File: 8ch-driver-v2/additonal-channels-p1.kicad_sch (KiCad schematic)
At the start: 42 parts, among them Q3 2N7002E, Q4 2N7002E, Q5 2N7002E, U3 DRV104PWP, U4 DRV104PWP, U5 DRV104PWP

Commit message: progress
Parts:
- renumbered Q5 to Q3, Q3 to Q5
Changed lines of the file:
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@@
 		(dnp no)
 		(fields_autoplaced yes)
-		(property "Reference" "Q5"
+		(property "Reference" "Q3"
 			(at 34.29 181.61 0)
 			(effects
@@
 			(project "8ch-driver-v2"
 				(path "/a0da8170-9d86-479a-b2aa-1f6179555439/fa1b9fcd-d6e8-44ab-a3c7-d4c590cf5d5a"
-					(reference "Q5")
+					(reference "Q3")
 					(unit 1)
 				)
@@
 		(dnp no)
 		(fields_autoplaced yes)
-		(property "Reference" "Q3"
+		(property "Reference" "Q5"
 			(at 33.02 73.66 0)
 			(effects
@@
 			(project "8ch-driver-v2"
 				(path "/a0da8170-9d86-479a-b2aa-1f6179555439/fa1b9fcd-d6e8-44ab-a3c7-d4c590cf5d5a"
-					(reference "Q3")
+					(reference "Q5")
 					(unit 1)
 				)

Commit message: mucho mas progresso
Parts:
- removed C10, C13, C16: 10uF, Capacitor_SMD:C_1210_3225Metric, symbol Device:C
- removed C11, C14, C8: 0.18uF, Capacitor_SMD:C_1206_3216Metric, symbol Device:C_Small
- removed C12, C15, C9: 470pF, Capacitor_SMD:C_1206_3216Metric, symbol Device:C_Small
- removed D10, D6, D8: PMEG10010ELRX, Diode_SMD:Nexperia_CFP3_SOD-123W, symbol Device:D
- removed D19, D20, D21: LED Green, LED_SMD:LED_0805_2012Metric, symbol Device:LED
- removed D7, D9: LED, LED_SMD:LED_0805_2012Metric, symbol Device:LED
- removed Q3, Q4, Q5: 2N7002E, Package_TO_SOT_SMD:SOT-23, symbol Transistor_FET:2N7002E
- removed R13, R17, R18, R22, R23: 4k7, Resistor_SMD:R_1206_3216Metric, symbol Device:R_US
- removed R14, R19, R24: 162k, Resistor_SMD:R_1206_3216Metric, symbol Device:R_US
- removed R15, R20, R25: 191k, Resistor_SMD:R_1206_3216Metric, symbol Device:R_US
- removed R16, R21: 49R9, Resistor_SMD:R_1206_3216Metric, symbol Device:R_US
- removed R43, R44, R45: 10K, Resistor_SMD:R_1206_3216Metric, symbol Device:R_US
- removed U3, U4, U5: DRV104PWP, Solenoid_Driver:IC_TPS27S100BPWPR, symbol DRV104PWP:DRV104PWP
- added C5: 10uF, Capacitor_SMD:C_1210_3225Metric, symbol Device:C
- added C6: 0.18uF, Capacitor_SMD:C_1206_3216Metric, symbol Device:C_Small
- added C7: 470pF, Capacitor_SMD:C_1206_3216Metric, symbol Device:C_Small
- added D4: PMEG10010ELRX, Diode_SMD:Nexperia_CFP3_SOD-123W, symbol Device:D
- added D6: LED, LED_SMD:LED_0805_2012Metric, symbol Device:LED
- added Q2: 2N7002E, Package_TO_SOT_SMD:SOT-23, symbol Transistor_FET:2N7002E
- added R10: 4k7, Resistor_SMD:R_1206_3216Metric, symbol Device:R_US
- added R7: 10K, Resistor_SMD:R_1206_3216Metric, symbol Device:R_US
- added R8: 162k, Resistor_SMD:R_1206_3216Metric, symbol Device:R_US
- added R9: 49R9, Resistor_SMD:R_1206_3216Metric, symbol Device:R_US
- added U2: DRV104PWP, Solenoid_Driver:IC_TPS27S100BPWPR, symbol DRV104PWP:DRV104PWP
- D5: value LED -> LED Green
- R11: value 49R9 -> 191k; PartNum RC0805FR-0749R9L -> RC0805FR-07191KL
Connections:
- net Relay03 is gone; now on net GND: R11.1
- net +12V: now also C5.1, R7.1, U2.10 (+VS), U2.8 (VPS2), U2.9 (VPS1)
- net GND: now also C5.2, C6.1, C7.1, D4.2 (A), Q2.2 (S), R10.1, R8.1, U2.11 (GND), U2.15 (EPAD)
- net at D5.2 (A): now also R7.2; no longer R12.2
- net fault3: no longer names the net of D5.1 (K)
- net fault3: now also Q2.3 (D)
- net in_term3 renamed freq03
- net freq03: now also U2.3 (OSC_FREQ_ADJ)
- new net: C7.2, U2.5 (BOOT)
- new net: D6.2 (A), R12.2
- new net DriveOut: D4.1 (K), U2.6 (OUT1), U2.7 (OUT2)
- new net TTLInput: R9.1
- new net delay03: C6.2, U2.2 (DELAY_ADJ)
- new net duty03: R8.2, U2.1 (DUTY_CYCLE_ADJ)
- new net fault03: D6.1 (K), U2.13 (STATUS_OK_FLAG)
- new net in_term03: Q2.1 (G), R10.2, R9.2, U2.14 (INPUT)
- no-connect marks 6 -> 2
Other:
- note added: "DRIVER6 ACTIVE LIGHT"
- note removed: "DRIVER3 ACTIVE LIGHT"
- note removed: "DRIVER4 ACTIVE LIGHT"
- note removed: "DRIVER5 ACTIVE LIGHT"

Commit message: push
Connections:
- net delay03 renamed delay
- net duty03 renamed duty
- net fault03 renamed fault
- net freq03 renamed freq
- net in_term03: no longer names the net of Q2.1 (G), R10.2, R9.2, U2.14 (INPUT)
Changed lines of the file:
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@@
+	)
+	(junction
+		(at 57.785 38.1)
+		(diameter 0)
+		(color 0 0 0 0)
 	)
 	(junction
@@
 		(color 0 0 0 0)
 	)
+	(junction
+		(at 19.05 52.07)
+		(diameter 0)
+		(color 0 0 0 0)
+	)
 	(no_connect
 		(at 104.14 50.8)
@@
 	(wire
 		(pts
+			(xy 17.78 52.07) (xy 19.05 52.07)
+		)
+		(stroke
+			(width 0)
+			(type default)
+		)
+	)
+	(wire
+		(pts
 			(xy 154.94 22.86) (xy 154.94 25.4)
 		)
@@
 	(wire
 		(pts
-			(xy 55.372 38.1) (xy 61.722 38.1)
+			(xy 55.372 38.1) (xy 57.785 38.1)
 		)
 		(stroke
@@
 	(wire
 		(pts
-			(xy 17.78 52.07) (xy 19.05 52.07)
+			(xy 57.785 52.07) (xy 57.785 38.1)
 		)
 		(stroke
@@
 	(wire
 		(pts
+			(xy 57.785 38.1) (xy 61.722 38.1)
+		)
+		(stroke
+			(width 0)
+			(type default)
+		)
+	)
+	(wire
+		(pts
 			(xy 61.722 38.1) (xy 61.722 39.37)
 		)
@@
 	(wire
 		(pts
+			(xy 19.05 52.07) (xy 57.785 52.07)
+		)
+		(stroke
+			(width 0)
+			(type default)
+		)
+	)
+	(wire
+		(pts
 			(xy 99.06 55.88) (xy 104.14 55.88)
 		)
@@
 		)
 	)
-	(label "fault03"
+	(hierarchical_label "freq"
+		(shape input)
+		(at 99.06 55.88 0)
+		(fields_autoplaced yes)
+		(effects
+			(font
+				(size 1.27 1.27)
+			)
+			(justify left)
+		)
+	)
+	(hierarchical_label "fault"
+		(shape input)
 		(at 99.06 60.96 0)
 		(fields_autoplaced yes)
@@
 				(size 1.27 1.27)
 			)
-			(justify left bottom)
-		)
-	)
-	(label "duty03"
-		(at 99.06 35.56 0)
-		(fields_autoplaced yes)
-		(effects
-			(font
-				(size 1.27 1.27)
-			)
-			(justify left bottom)
-		)
-	)
-	(label "freq03"
-		(at 99.06 55.88 0)
-		(fields_autoplaced yes)
-		(effects
-			(font
-				(size 1.27 1.27)
-			)
-			(justify left bottom)
-		)
-	)
-	(label "in_term03"
-		(at 78.486 38.1 0)
-		(fields_autoplaced yes)
-		(effects
-			(font
-				(size 1.27 1.27)
-			)
-			(justify left bottom)
-		)
-	)
-	(label "in_term03"
-		(at 17.78 52.07 90)
-		(fields_autoplaced yes)
-		(effects
-			(font
-				(size 1.27 1.27)
-			)
-			(justify left bottom)
-		)
-	)
-	(label "delay03"
-		(at 99.06 33.02 0)
-		(fields_autoplaced yes)
-		(effects
-			(font
-				(size 1.27 1.27)
-			)
-			(justify left bottom)
+			(justify left)
 		)
 	)
@@
 		)
 	)
+	(hierarchical_label "duty"
+		(shape input)
+		(at 99.06 35.56 0)
+		(fields_autoplaced yes)
+		(effects
+			(font
+				(size 1.27 1.27)
+			)
+			(justify left)
+		)
+	)
 	(hierarchical_label "DriveOut"
 		(shape output)
@@
 		(fields_autoplaced yes)
 		(effects
+			(font
+				(size 1.27 1.27)
+			)
+			(justify left)
+		)
+	)
+	(hierarchical_label "delay"
+		(shape input)
+		(at 99.06 33.02 0)
+		(fields_autoplaced yes)
+		(effects

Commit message: push
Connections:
- net GND: now also U2.16 (GND), U2.17 (GND), U2.18 (GND), U2.19 (GND), U2.20 (GND)
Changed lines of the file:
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@@
+	)
+	(junction
+		(at 154.94 66.04)
+		(diameter 0)
+		(color 0 0 0 0)
+	)
+	(junction
+		(at 152.4 63.5)
+		(diameter 0)
+		(color 0 0 0 0)
 	)
 	(junction
@@
 	)
 	(junction
+		(at 152.4 55.88)
+		(diameter 0)
+		(color 0 0 0 0)
+	)
+	(junction
 		(at 154.94 25.4)
+		(diameter 0)
+		(color 0 0 0 0)
+	)
+	(junction
+		(at 152.4 58.42)
 		(diameter 0)
 		(color 0 0 0 0)
@@
 	)
 	(junction
+		(at 152.4 60.96)
+		(diameter 0)
+		(color 0 0 0 0)
+	)
+	(junction
 		(at 154.94 22.86)
 		(diameter 0)
@@
 	(wire
 		(pts
+			(xy 156.21 63.5) (xy 156.21 66.04)
+		)
+		(stroke
+			(width 0)
+			(type default)
+		)
+	)
+	(wire
+		(pts
 			(xy 78.105 60.96) (xy 104.14 60.96)
 		)
@@
 	(wire
 		(pts
+			(xy 152.4 63.5) (xy 156.21 63.5)
+		)
+		(stroke
+			(width 0)
+			(type default)
+		)
+	)
+	(wire
+		(pts
+			(xy 156.21 66.04) (xy 154.94 66.04)
+		)
+		(stroke
+			(width 0)
+			(type default)
+		)
+	)
+	(wire
+		(pts
+			(xy 152.4 55.88) (xy 152.4 58.42)
+		)
+		(stroke
+			(width 0)
+			(type default)
+		)
+	)
+	(wire
+		(pts
 			(xy 163.83 43.18) (xy 158.75 43.18)
 		)
@@
 	(wire
 		(pts
+			(xy 152.4 60.96) (xy 152.4 63.5)
+		)
+		(stroke
+			(width 0)
+			(type default)
+		)
+	)
+	(wire
+		(pts
 			(xy 26.67 45.72) (xy 26.67 46.99)
 		)
@@
 	(wire
 		(pts
+			(xy 152.4 53.34) (xy 152.4 55.88)
+		)
+		(stroke
+			(width 0)
+			(type default)
+		)
+	)
+	(wire
+		(pts
 			(xy 154.94 68.58) (xy 154.94 70.485)
 		)
@@
 		(pts
 			(xy 154.94 33.02) (xy 154.94 35.56)
+		)
+		(stroke
+			(width 0)
+			(type default)
+		)
+	)
+	(wire
+		(pts
+			(xy 152.4 58.42) (xy 152.4 60.96)
 		)
 		(stroke
@@
 		(pin "9"
 		)
+		(pin "16"
+		)
+		(pin "17"
+		)
+		(pin "18"
+		)
+		(pin "19"
+		)
+		(pin "20"
+		)
 		(instances

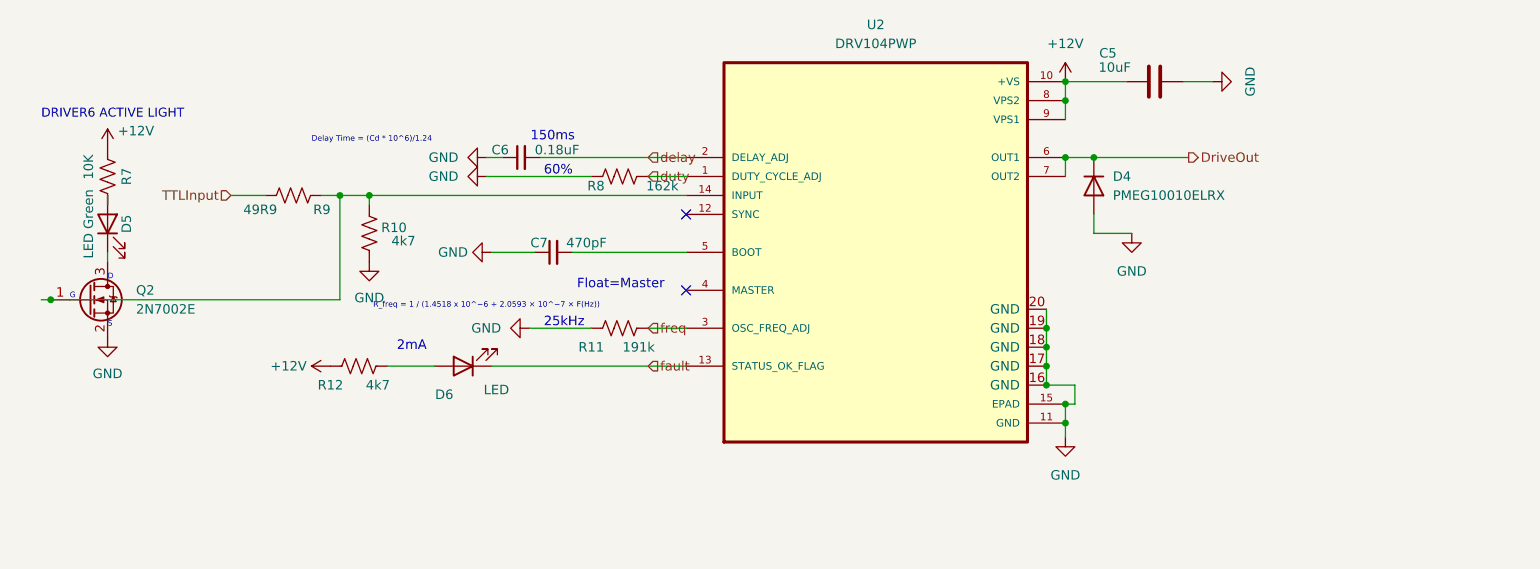
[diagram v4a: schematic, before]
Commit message: 16-valve PCB layout for inspection
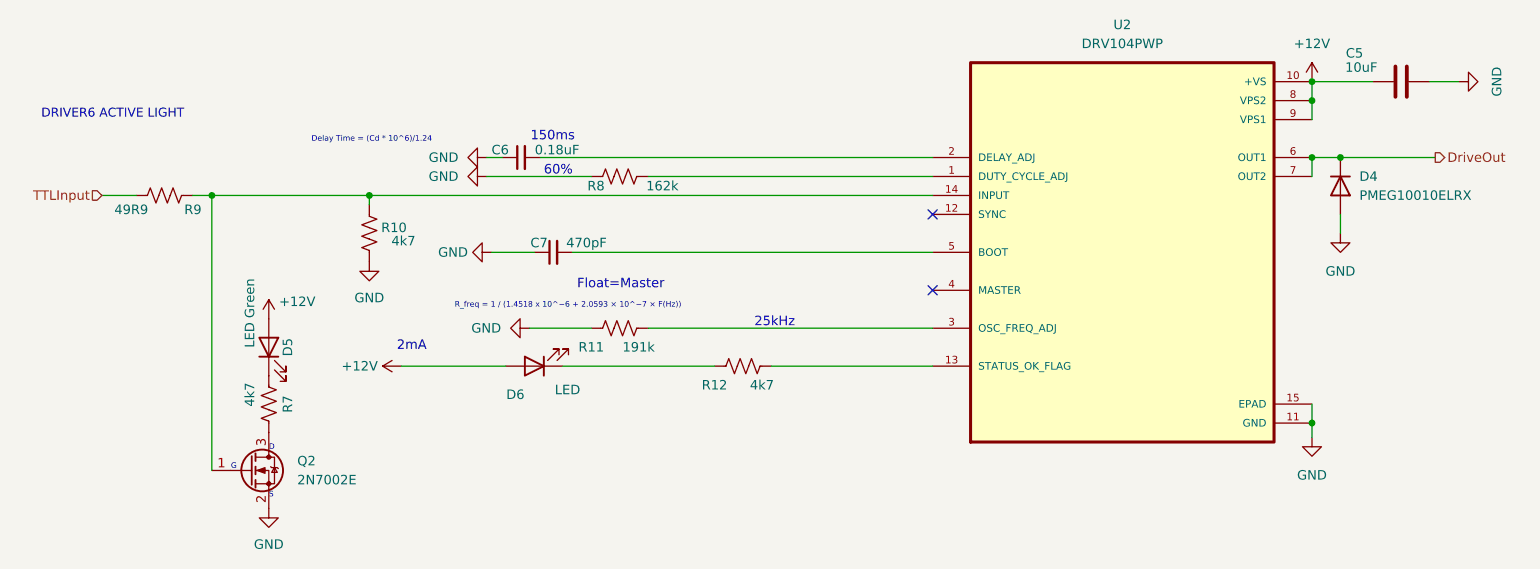
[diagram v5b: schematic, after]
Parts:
- R7: value 10K -> 4k7
- U2: footprint Solenoid_Driver:IC_TPS27S100BPWPR -> footprint:IC_TPS27S100BPWPR
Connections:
- net +12V: now also D5.2 (A), D6.2 (A); no longer R12.1, R7.1
- net GND: no longer U2.16 (GND), U2.17 (GND), U2.18 (GND), U2.19 (GND), U2.20 (GND)
- net at R7.2: now also Q2.3 (D); no longer D5.2 (A)
- net at R12.2: now also U2.13 (STATUS_OK_FLAG); no longer D6.2 (A)
- net at D5.1 (K): now also R7.1; no longer Q2.3 (D)
- net delay: no longer names the net of C6.2, U2.2 (DELAY_ADJ)
- net duty: no longer names the net of R8.2, U2.1 (DUTY_CYCLE_ADJ)
- net fault: no longer names the net of D6.1 (K)
- net fault: now also R12.1; no longer U2.13 (STATUS_OK_FLAG)
- net freq: no longer names the net of R11.2, U2.3 (OSC_FREQ_ADJ)
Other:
- moved on the sheet: C5, D4, D5, D6, Q2, R12, R7, R9
